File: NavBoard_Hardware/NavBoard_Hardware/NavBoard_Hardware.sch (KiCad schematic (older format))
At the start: 62 parts

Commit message: Assigned footprints and started layout
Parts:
- AC1: renamed from AC?; footprint BNO080 -> BNO080:BNO080
- BT1: renamed from BT?; footprint (none) -> Battery:BatteryHolder_Keystone_3008_1x2450
- C1, C4: renamed from C?; footprint (none) -> Capacitor_THT:CP_Radial_D6.3mm_P2.50mm
- C10, C11, C12, C13, C14, C15, C16, C17, C2, C3, C5, C6, C7, C8, C9: renamed from C?; footprint (none) -> Capacitor_SMD:C_0603_1608Metric_Pad1.08x0.95mm_HandSolder
- Conn1: renamed from Conn?; footprint (none) -> MRDT_Connectors:Anderson_2_Horizontal_Side_by_Side
- Conn2: renamed from Conn?; footprint (none) -> MRDT_Connectors:RP-SMA_Jack_Tru-Hole_Right-Angle
- D1, D10, D11, D12, D2, D3, D4, D5, D6, D7, D8, D9: renamed from D?; footprint (none) -> LED_SMD:LED_0603_1608Metric_Pad1.05x0.95mm_HandSolder
- R1, R10, R11, R12, R13, R14, R15, R16, R17, R18, R19, R2, R20, R21, R22, R3, R4, R5, R6, R7, R8, R9: renamed from R?; footprint (none) -> Resistor_SMD:R_0603_1608Metric_Pad0.98x0.95mm_HandSolder
- U1, U4: renamed from U?; footprint (none) -> MRDT_Devices:OKI_Horizontal
- U2: renamed from U?; footprint MRDT_ICs:QFN40P300X300X105-24N -> MRDT_ICs:ICM_20948
- U3: renamed from U?; footprint MRDT_ICs:LGA28R50P4X10_380X520X100 -> MRDT_ICs:BNO055
- U6: renamed from U?; footprint (none) -> MRDT_Shields:RaspberryPi_THT_BOTTOM
- gave numbers to parts that had none: 1

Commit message: Deleted old components
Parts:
- removed AC1: BNO080, BNO080:BNO080, symbol NavBoard_Hardware-rescue:BNO080-BNO080
- removed BT1: Battery_Cell, Battery:BatteryHolder_Keystone_3008_1x2450, symbol Device:Battery_Cell
- removed C10, C11, C12, C14, C15, C16, C9: 0.1uF, Capacitor_SMD:C_0603_1608Metric_Pad1.08x0.95mm_HandSolder, symbol Device:C
- removed C13: 1uF, Capacitor_SMD:C_0603_1608Metric_Pad1.08x0.95mm_HandSolder, symbol Device:C
- removed C17: 47pF, Capacitor_SMD:C_0603_1608Metric_Pad1.08x0.95mm_HandSolder, symbol Device:C
- removed C7: 6.8nF, Capacitor_SMD:C_0603_1608Metric_Pad1.08x0.95mm_HandSolder, symbol Device:C
- removed C8: 120nF, Capacitor_SMD:C_0603_1608Metric_Pad1.08x0.95mm_HandSolder, symbol Device:C
- removed Conn2: RP-SMA, MRDT_Connectors:RP-SMA_Jack_Tru-Hole_Right-Angle, symbol NavBoard_Hardware-rescue:RP-SMA-MRDT_Connectors
- removed D10, D11, D12, D3, D4, D5, D6, D7, D8, D9: BLUE, LED_SMD:LED_0603_1608Metric_Pad1.05x0.95mm_HandSolder, symbol Device:LED
- removed R1: 10K, Resistor_SMD:R_0603_1608Metric_Pad0.98x0.95mm_HandSolder, symbol Device:R
- removed R10, R6, R8: 2.2k, Resistor_SMD:R_0603_1608Metric_Pad0.98x0.95mm_HandSolder, symbol Device:R
- removed R13, R14, R15, R16, R17, R18, R19, R20, R21, R22: 100, Resistor_SMD:R_0603_1608Metric_Pad0.98x0.95mm_HandSolder, symbol Device:R
- removed R2: 10, Resistor_SMD:R_0603_1608Metric_Pad0.98x0.95mm_HandSolder, symbol Device:R
- removed R3: 30@100MHZ/2.0A, Resistor_SMD:R_0603_1608Metric_Pad0.98x0.95mm_HandSolder, symbol Device:R
- removed R4, R5, R7, R9: 10k, Resistor_SMD:R_0603_1608Metric_Pad0.98x0.95mm_HandSolder, symbol Device:R
- removed U2: ICM-20948, MRDT_ICs:ICM_20948, symbol NavBoard_Hardware-rescue:ICM-20948-MRDT_ICs
- removed U3: BNO055, MRDT_ICs:BNO055, symbol NavBoard_Hardware-rescue:BNO055-MRDT_ICs
- removed U5: NEO-M8P-2, MRDT_ICs:MODULE_NEO-M8P-2, symbol NavBoard_Hardware-rescue:NEO-M8P-2-MRDT_ICs
- renumbered R11 to R?, R12 to R?
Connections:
- net BNO055_RX: no longer names the net of U6.8 (GP_14)
- net BNO055_TX: no longer names the net of U6.10 (GP_15)
- net BNO080_SCL: no longer names the net of U6.5 (GP_3)
- net BNO080_SDA: no longer names the net of U6.3 (GP_2)
- net ICM_CS: no longer names the net of U6.12 (GP_18)
- net ICM_MISO: no longer names the net of U6.21 (GP_9)
- net ICM_MOSI: no longer names the net of U6.19 (GP_10)
- net ICM_SCLK: no longer names the net of U6.23 (GP_11)
- net M8P_CLK: no longer names the net of U6.40 (GP_21)
- net M8P_CS: no longer names the net of U6.36 (GP_16)
- net M8P_MISO: no longer names the net of U6.35 (GP_19)
- net M8P_MOSI: no longer names the net of U6.38 (GP_20)
- no-connect marks 50 -> 18
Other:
- moved on the sheet: C1, C2, C3, C4, C5, C6, Conn1A, Conn1B, U6

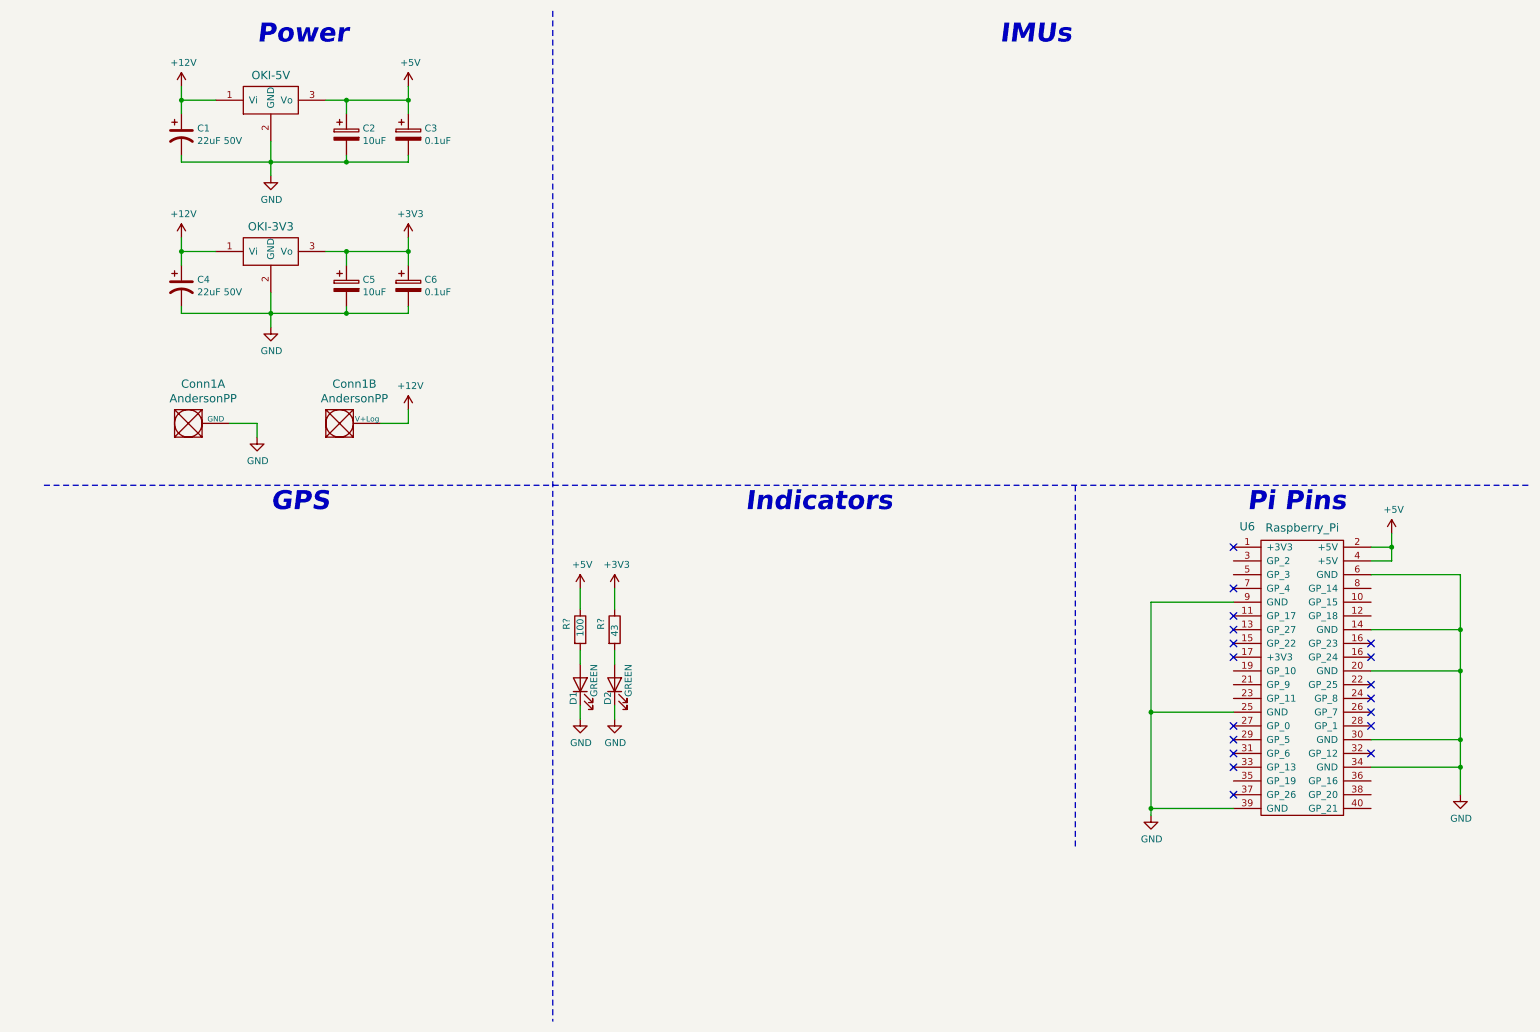
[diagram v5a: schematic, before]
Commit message: Downloaded footprints and libraries, wired GPS
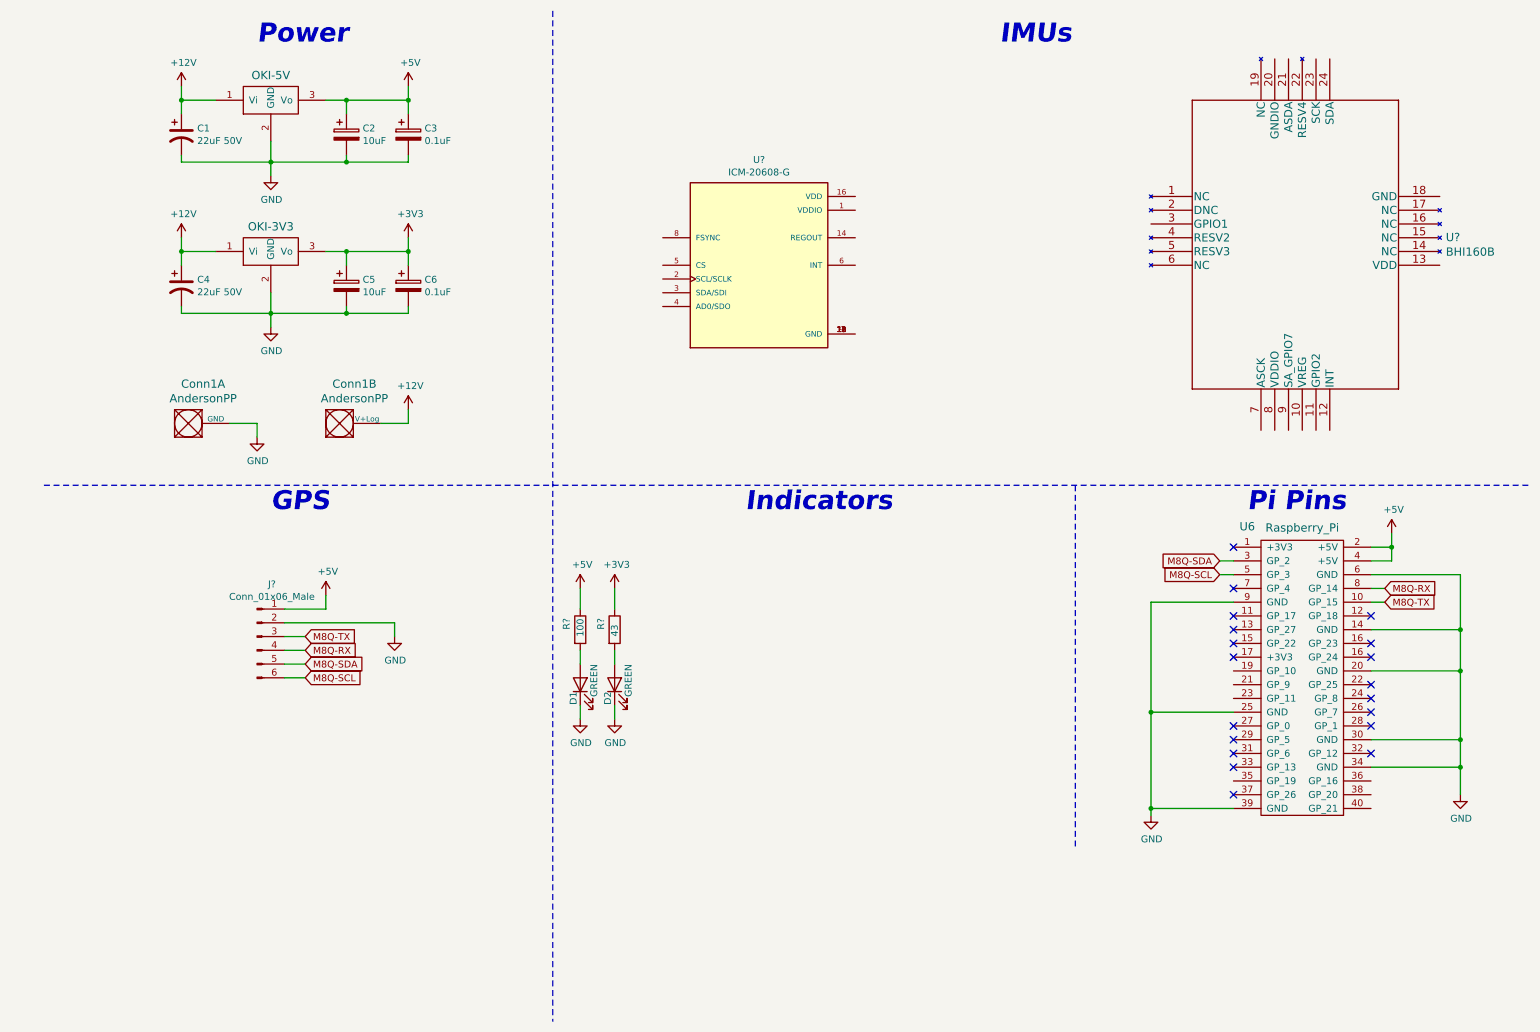
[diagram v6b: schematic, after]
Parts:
- added J?: Conn_01x06_Male, symbol Connector:Conn_01x06_Male
- added U?: ICM-20608-G, PQFN50P300X300X80-16N, symbol ICM-20608-G:ICM-20608-G
- added U?: BHI160B, LGA24_3X3X0P95_3_BOS, symbol 2021-11-17_00-14-18:BHI160B
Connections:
- net +5V: now also J?.1 (Pin_1)
- net GND: now also J?.2 (Pin_2)
- net M8Q-TX: now reaches U6.10 (GP_15)
- net M8Q-TX: now also J?.3 (Pin_3)
- net M8Q-SDA: now reaches U6.3 (GP_2)
- net M8Q-SDA: now also J?.5 (Pin_5)
- net M8Q-SCL: now reaches U6.5 (GP_3)
- net M8Q-SCL: now also J?.6 (Pin_6)
- net M8Q-RX: now reaches U6.8 (GP_14)
- net M8Q-RX: now also J?.4 (Pin_4)
- new net: U?.10 (GND), U?.11 (GND), U?.12 (GND), U?.13 (GND), U?.15 (GND), U?.9 (GND)
- no-connect marks 18 -> 19
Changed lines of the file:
@@
 	4150 450  4150 7800
 Connection ~ 1450 2200
+$Comp
+L Connector:Conn_01x06_Male J?
+U 1 1 61945DB8
+P 2000 5000
+F 0 "J?" H 2108 5381 50  0000 C CNN
+F 1 "Conn_01x06_Male" H 2108 5290 50  0000 C CNN
+F 2 "" H 2000 5000 50  0001 C CNN
+F 3 "~" H 2000 5000 50  0001 C CNN
+	1    2000 5000
+	1    0    0    -1
+$EndComp
+$Comp
+L power:+5V #PWR?
+U 1 1 61946E05
+P 2500 4700
+F 0 "#PWR?" H 2500 4550 50  0001 C CNN
+F 1 "+5V" H 2515 4873 50  0000 C CNN
+F 2 "" H 2500 4700 50  0001 C CNN
+F 3 "" H 2500 4700 50  0001 C CNN
+	1    2500 4700
+	1    0    0    -1
+$EndComp
+$Comp
+L power:GND #PWR?
+U 1 1 61947658
+P 3000 5000
+F 0 "#PWR?" H 3000 4750 50  0001 C CNN
+F 1 "GND" H 3005 4827 50  0000 C CNN
+F 2 "" H 3000 5000 50  0001 C CNN
+F 3 "" H 3000 5000 50  0001 C CNN
+	1    3000 5000
+	1    0    0    -1
+$EndComp
+Text GLabel 2350 5000 2    50   Input ~ 0
+M8Q-TX
+Text GLabel 2350 5100 2    50   Input ~ 0
+M8Q-RX
+Text GLabel 2350 5200 2    50   Input ~ 0
+M8Q-SDA
+Text GLabel 2350 5300 2    50   Input ~ 0
+M8Q-SCL
+Wire Wire Line
+	2350 5000 2200 5000
+Wire Wire Line
+	2200 5100 2350 5100
+Wire Wire Line
+	2350 5200 2200 5200
+Wire Wire Line
+	2200 5300 2350 5300
+Wire Wire Line
+	2500 4700 2500 4800
+Wire Wire Line
+	2500 4800 2200 4800
+Wire Wire Line
+	2200 4900 3000 4900
+Wire Wire Line
+	3000 4900 3000 5000
+Text GLabel 10200 4750 2    50   Input ~ 0
+M8Q-TX
+Text GLabel 10200 4650 2    50   Input ~ 0
+M8Q-RX
+Wire Wire Line
+	10200 4750 10100 4750
+Wire Wire Line
+	10200 4650 10100 4650
+NoConn ~ 10100 4850
+Text GLabel 9000 4450 0    50   Input ~ 0
+M8Q-SDA
+Text GLabel 9000 4550 0    50   Input ~ 0
+M8Q-SCL
+Wire Wire Line
+	9000 4450 9100 4450
+Wire Wire Line
+	9100 4550 9000 4550
+$Comp
+L ICM-20608-G:ICM-20608-G U?
+U 1 1 619643F9
+P 5650 2300
+F 0 "U?" H 5650 3067 50  0000 C CNN
+F 1 "ICM-20608-G" H 5650 2976 50  0000 C CNN
+F 2 "PQFN50P300X300X80-16N" H 5650 2300 50  0001 L BNN
+F 3 "" H 5650 2300 50  0001 L BNN
+F 4 "TDK" H 5650 2300 50  0001 L BNN "MANUFACTURER"
+F 5 "1.0" H 5650 2300 50  0001 L BNN "PARTREV"
+F 6 "IPC-7351B" H 5650 2300 50  0001 L BNN "STANDARD"
+	1    5650 2300
+	1    0    0    -1
+$EndComp
+$Comp
+L 2021-11-17_00-14-18:BHI160B U?
+U 1 1 619661AC
+P 8500 1800
+F 0 "U?" H 10644 1503 60  0000 L CNN
+F 1 "BHI160B" H 10644 1397 60  0000 L CNN
+F 2 "LGA24_3X3X0P95_3_BOS" H 9300 2540 60  0001 C CNN
+F 3 "" H 8500 1800 60  0000 C CNN
+	1    8500 1800
+	1    0    0    -1
+$EndComp
 $EndSCHEMATC

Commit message: Completed schematic
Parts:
- added C10: 10nF, symbol Device:C
- added C11, C12: 0.47uF, symbol Device:C
- added C13: 1uF, symbol Device:C
- added C14, C7, C9: 0.1uF, symbol Device:C
- added C8: 2.2uF, symbol Device:C
- added D10, D3, D4, D5, D6, D7, D8, D9: BLUE, LED_SMD:LED_0603_1608Metric_Pad1.05x0.95mm_HandSolder, symbol Device:LED
- added R10, R3, R4, R5, R6, R7, R8, R9: 100, Resistor_SMD:R_0603_1608Metric_Pad0.98x0.95mm_HandSolder, symbol Device:R
- gave numbers to parts that had none: 5
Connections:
- net M8Q-SCL is gone; now on net I2C-SCL: J1.6 (Pin_6), U6.5 (GP_3)
- net M8Q-SDA is gone; now on net I2C-SDA: J1.5 (Pin_5), U6.3 (GP_2)
- net +3V3: now also U2.13 (VDD), U2.8 (VDDIO), U3.1 (VDDIO), C10.1, C13.1, C14.1, C7.1, C8.1, C9.2
- net GND: now also U2.18 (GND), U2.20 (GNDIO), U2.9 (SA_GPIO7), U3.10 (GND), U3.11 (GND), U3.12 (GND), U3.13 (GND), U3.15 (GND), U3.8 (FSYNC), U3.9 (GND), C10.2, C11.2, C12.2, C13.2, C14.2, C9.1, D10.1 (K), D3.1 (K), D4.1 (K), D5.1 (K), D6.1 (K), D7.1 (K), D8.1 (K), D9.1 (K)
- net M8Q-RX: now also R5.1
- net M8Q-TX: now also R6.1
- net ICM-SDI: now reaches U6.19 (GP_10)
- net ICM-SDI: now also U3.3 (SDA/SDI), R7.1
- net ICM-SDO: now reaches U6.21 (GP_9)
- net ICM-SDO: now also U3.4 (AD0/SDO), R8.1
- net ICM-SCLK: now reaches U6.23 (GP_11)
- net ICM-SCLK: now also U3.2 (SCL/SCLK), R9.1
- net ICM-CS: now reaches U6.24 (GP_8)
- net ICM-CS: now also U3.5 (CS), R10.1
- net at U3.14 (REGOUT): now also C11.1
- net at U3.16 (VDD): now also C7.2, C8.2
- net at U2.10 (VREG): now also C12.1
- net I2C-SCL: now reaches U2.23 (SCK)
- net I2C-SCL: now also R4.1
- net I2C-SDA: now reaches U2.24 (SDA)
- net I2C-SDA: now also R3.1
- new net: D3.2 (A), R3.2
- new net: D4.2 (A), R4.2
- new net: D5.2 (A), R5.2
- new net: D6.2 (A), R6.2
- new net: D7.2 (A), R7.2
- new net: D8.2 (A), R8.2
- new net: D9.2 (A), R9.2
- new net: D10.2 (A), R10.2
- no-connect marks 19 -> 24
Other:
- moved on the sheet: C1, C2, C3, C4, C5, C6, Conn1A, Conn1B, D1, D2, J1, R1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
